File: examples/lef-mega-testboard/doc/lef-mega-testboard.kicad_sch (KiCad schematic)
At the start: 20 parts, among them J1 HD44780, SW1 RotaryEncoder_Switch, SW2 SW_Push, SW3 SW_Push, SW4 SW_Push

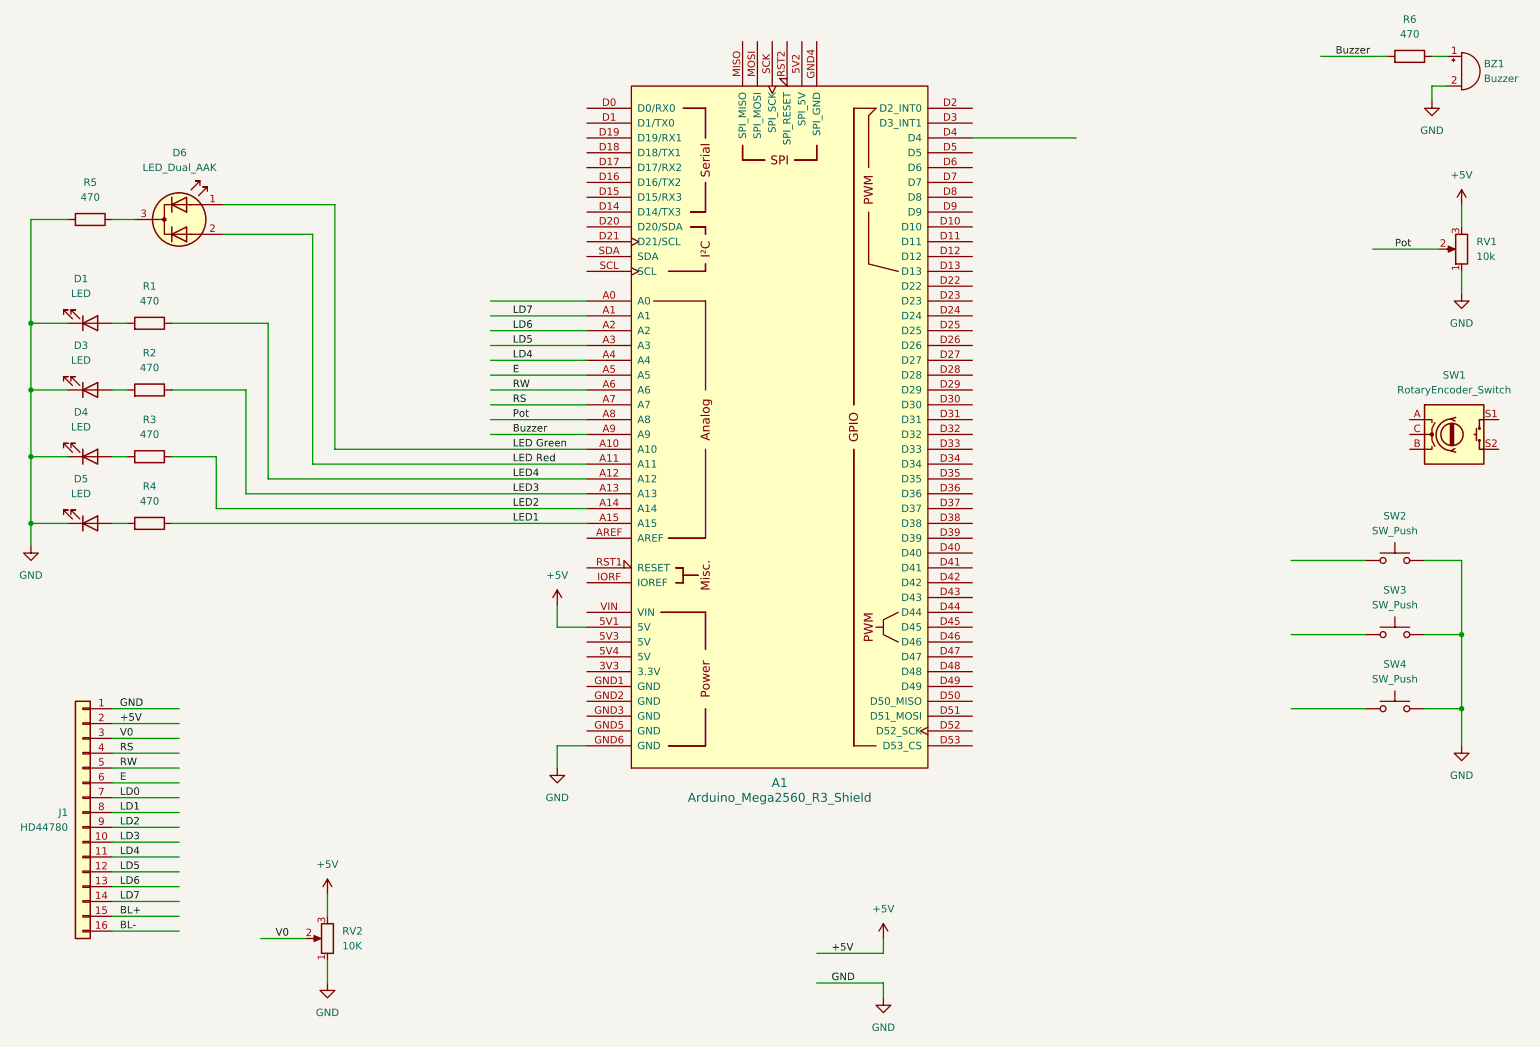
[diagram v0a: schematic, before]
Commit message: Added generic 16 bit timer
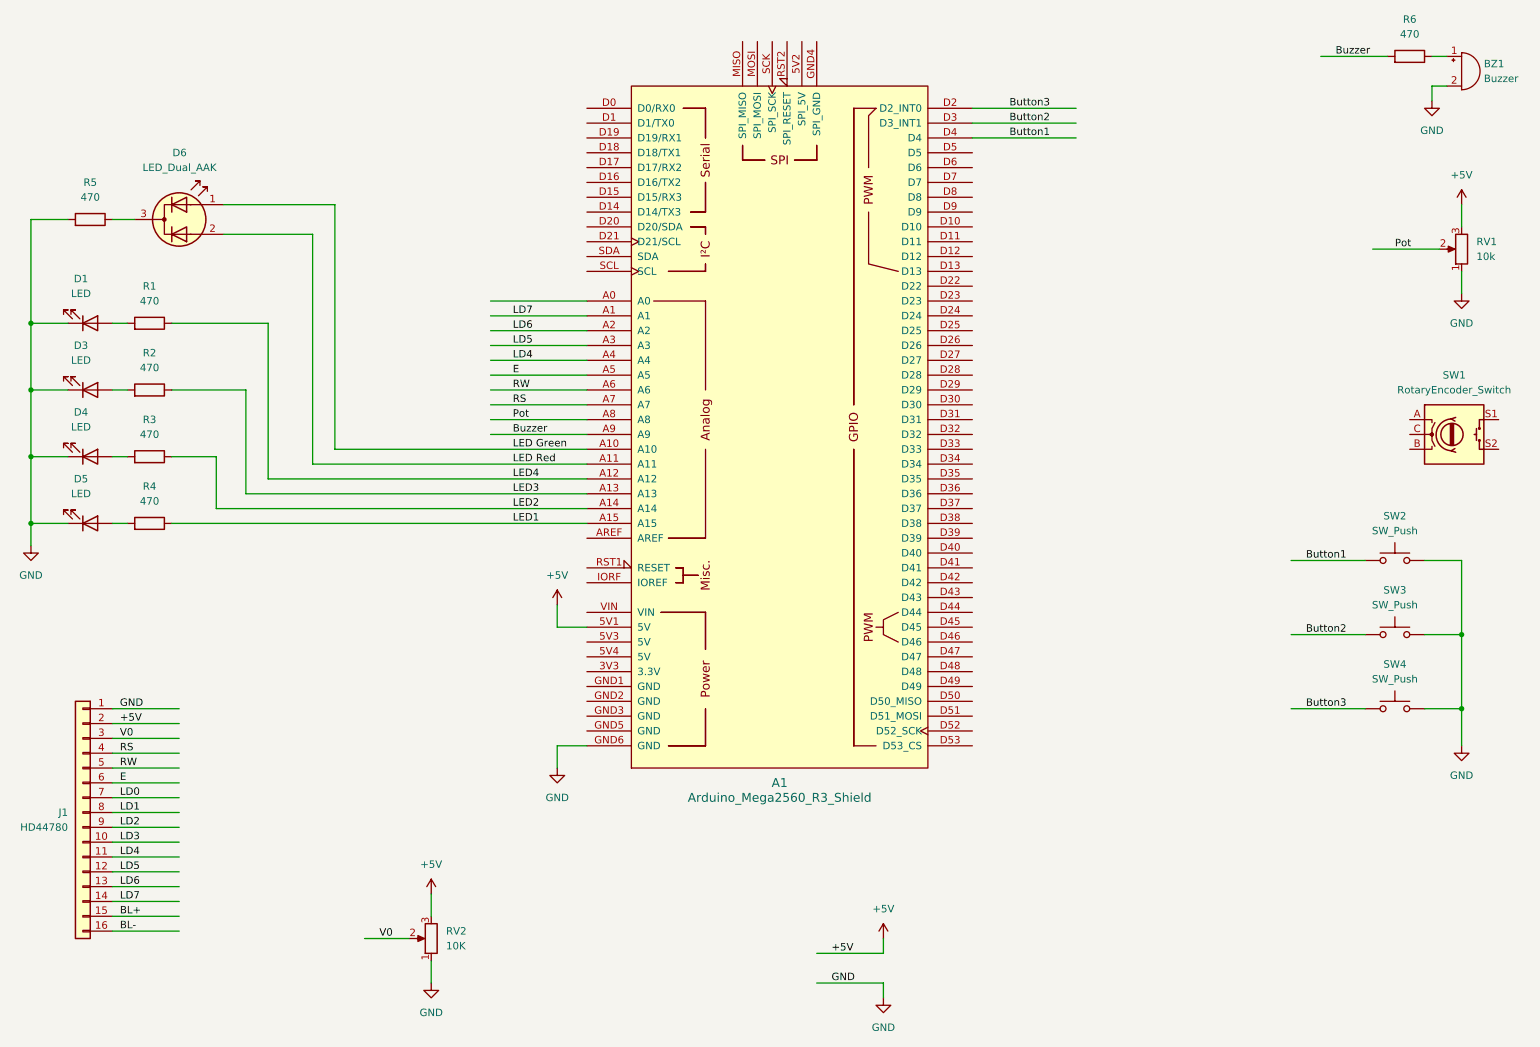
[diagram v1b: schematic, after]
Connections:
- net Button1: now reaches SW2.1
- net Button1: now also A1.D4
- net Button2: now reaches SW3.1
- net Button2: now also A1.D3 (D3_INT1)
- net Button3: now reaches SW4.1
- net Button3: now also A1.D2 (D2_INT0)
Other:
- moved on the sheet: RV2
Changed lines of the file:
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@@
 	(wire
 		(pts
-			(xy 71.12 176.53) (xy 71.12 172.72)
+			(xy 88.9 176.53) (xy 88.9 172.72)
 		)
 		(stroke
@@
 	(wire
 		(pts
-			(xy 71.12 187.96) (xy 71.12 184.15)
+			(xy 88.9 187.96) (xy 88.9 184.15)
+		)
+		(stroke
+			(width 0)
+			(type default)
+		)
+	)
+	(wire
+		(pts
+			(xy 181.61 38.1) (xy 199.39 38.1)
 		)
 		(stroke
@@
 	(wire
 		(pts
-			(xy 59.69 180.34) (xy 67.31 180.34)
+			(xy 77.47 180.34) (xy 85.09 180.34)
 		)
 		(stroke
@@
 	(wire
 		(pts
+			(xy 181.61 40.64) (xy 199.39 40.64)
+		)
+		(stroke
+			(width 0)
+			(type default)
+		)
+	)
+	(wire
+		(pts
 			(xy 60.96 101.6) (xy 115.57 101.6)
 		)
@@
 		)
 	)
+	(label "Button2"
+		(at 238.76 128.27 0)
+		(effects
+			(font
+				(size 1.27 1.27)
+			)
+			(justify left bottom)
+		)
+	)
 	(label "LD6"
 		(at 35.56 171.45 0)
@@
 		)
 	)
+	(label "Button1"
+		(at 238.76 115.57 0)
+		(effects
+			(font
+				(size 1.27 1.27)
+			)
+			(justify left bottom)
+		)
+	)
 	(label "GND"
 		(at 35.56 140.97 0)
@@
 		)
 	)
+	(label "Button2"
+		(at 187.96 40.64 0)
+		(effects
+			(font
+				(size 1.27 1.27)
+			)
+			(justify left bottom)
+		)
+	)
 	(label "+5V"
 		(at 157.48 182.88 0)
@@
 		)
 	)
+	(label "Button3"
+		(at 187.96 38.1 0)
+		(effects
+			(font
+				(size 1.27 1.27)
+			)
+			(justify left bottom)
+		)
+	)
 	(label "LD4"
 		(at 102.87 81.28 0)
@@
 	)
 	(label "V0"
-		(at 62.23 180.34 0)
+		(at 80.01 180.34 0)
 		(effects
 			(font
@@
 		)
 	)
+	(label "Button3"
+		(at 238.76 140.97 0)
+		(effects
+			(font
+				(size 1.27 1.27)
+			)
+			(justify left bottom)
+		)
+	)
 	(label "LD2"
 		(at 35.56 161.29 0)
@@
 		)
 	)
+	(label "Button1"
+		(at 187.96 43.18 0)
+		(effects
+			(font
+				(size 1.27 1.27)
+			)
+			(justify left bottom)
+		)
+	)
 	(symbol
 		(lib_id "power:GND")
@@
 		)
 		(instances
-			(project ""
+			(project "lef-mega-testboard"
 				(path "/23172db6-2709-4b02-aaae-9ed28b7e74f3"
 					(reference "BZ1")
@@
 	(symbol
 		(lib_id "power:+5V")
-		(at 71.12 172.72 0)
+		(at 88.9 172.72 0)
 		(unit 1)
 		(exclude_from_sim no)
@@
 		(fields_autoplaced yes)
 		(property "Reference" "#PWR09"
-			(at 71.12 176.53 0)
+			(at 88.9 176.53 0)
 			(effects
 				(font
@@
 		)
 		(property "Value" "+5V"
-			(at 71.12 167.64 0)
+			(at 88.9 167.64 0)
 			(effects
 				(font
@@
 		)
 		(property "Footprint" ""
-			(at 71.12 172.72 0)
+			(at 88.9 172.72 0)
 			(effects
 				(font
@@
 		)
 		(property "Datasheet" ""
-			(at 71.12 172.72 0)
+			(at 88.9 172.72 0)
 			(effects
 				(font
@@
 		)
 		(property "Description" "Power symbol creates a global label with name \"+5V\""
-			(at 71.12 172.72 0)
+			(at 88.9 172.72 0)
 			(effects
 				(font
@@
 		)
 		(instances
-			(project ""
+			(project "lef-mega-testboard"
 				(path "/23172db6-2709-4b02-aaae-9ed28b7e74f3"
 					(reference "SW2")
@@
 	(symbol
 		(lib_id "power:GND")
-		(at 71.12 187.96 0)
+		(at 88.9 187.96 0)
 		(unit 1)
 		(exclude_from_sim no)
@@
 		(fields_autoplaced yes)
 		(property "Reference" "#PWR010"
-			(at 71.12 194.31 0)
+			(at 88.9 194.31 0)
 			(effects
 				(font
@@
 		)
 		(property "Value" "GND"
-			(at 71.12 193.04 0)
+			(at 88.9 193.04 0)
 			(effects
 				(font
@@
 		)
 		(property "Footprint" ""
-			(at 71.12 187.96 0)
+			(at 88.9 187.96 0)
 			(effects
 				(font
@@
 		)
 		(property "Datasheet" ""
-			(at 71.12 187.96 0)
+			(at 88.9 187.96 0)
 			(effects
 				(font
@@
 		)
 		(property "Description" "Power symbol creates a global label with name \"GND\" , ground"
-			(at 71.12 187.96 0)
+			(at 88.9 187.96 0)
 			(effects
 				(font
@@
 		)
 		(instances
-			(project ""
+			(project "lef-mega-testboard"
 				(path "/23172db6-2709-4b02-aaae-9ed28b7e74f3"
 					(reference "#PWR01")
@@
 		)
 		(instances
-			(project ""
+			(project "lef-mega-testboard"
 				(path "/23172db6-2709-4b02-aaae-9ed28b7e74f3"
 					(reference "SW1")
@@
 		)
 		(instances
-			(project ""
+			(project "lef-mega-testboard"
 				(path "/23172db6-2709-4b02-aaae-9ed28b7e74f3"
 					(reference "D1")
@@
 	(symbol
 		(lib_id "Device:R_Potentiometer")
-		(at 71.12 180.34 180)
+		(at 88.9 180.34 180)
 		(unit 1)
 		(exclude_from_sim no)
@@
 		(fields_autoplaced yes)
 		(property "Reference" "RV2"
-			(at 73.66 179.0699 0)
+			(at 91.44 179.0699 0)
 			(effects
 				(font
@@
 		)
 		(property "Value" "10K"
-			(at 73.66 181.6099 0)
+			(at 91.44 181.6099 0)
 			(effects
 				(font
@@
 		)
 		(property "Footprint" "Potentiometer_THT:Potentiometer_Alpha_RD902F-40-00D_Dual_Vertical"
-			(at 71.12 180.34 0)
+			(at 88.9 180.34 0)
 			(effects
 				(font
@@
 		)
 		(property "Datasheet" "~"
-			(at 71.12 180.34 0)
+			(at 88.9 180.34 0)
 			(effects
 				(font
@@
 		)
 		(property "Description" "Potentiometer"
-			(at 71.12 180.34 0)
+			(at 88.9 180.34 0)
 			(effects
 				(font
@@
 		)
 		(instances
-			(project ""
+			(project "lef-mega-testboard"
 				(path "/23172db6-2709-4b02-aaae-9ed28b7e74f3"
 					(reference "R1")
@@
 		)
 		(instances
-			(project ""
+			(project "lef-mega-testboard"
 				(path "/23172db6-2709-4b02-aaae-9ed28b7e74f3"
 					(reference "D6")
@@
 		)
 		(instances
-			(project ""
+			(project "lef-mega-testboard"
 				(path "/23172db6-2709-4b02-aaae-9ed28b7e74f3"
 					(reference "RV1")
@@
 		)
 		(instances
-			(project ""
+			(project "lef-mega-testboard"
 				(path "/23172db6-2709-4b02-aaae-9ed28b7e74f3"
 					(reference "A1")
@@
 		)
 		(instances
-			(project ""
+			(project "lef-mega-testboard"
 				(path "/23172db6-2709-4b02-aaae-9ed28b7e74f3"
 					(reference "#PWR02")
@@
 		)
 		(instances
-			(project ""
+			(project "lef-mega-testboard"
 				(path "/23172db6-2709-4b02-aaae-9ed28b7e74f3"
 					(reference "J1")
